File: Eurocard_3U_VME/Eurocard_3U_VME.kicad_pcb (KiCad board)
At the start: 2 copper layers, 100 x 160 mm, 1839 parts, among them J1 VG64_VME_3Rows_3x32_J1_P1

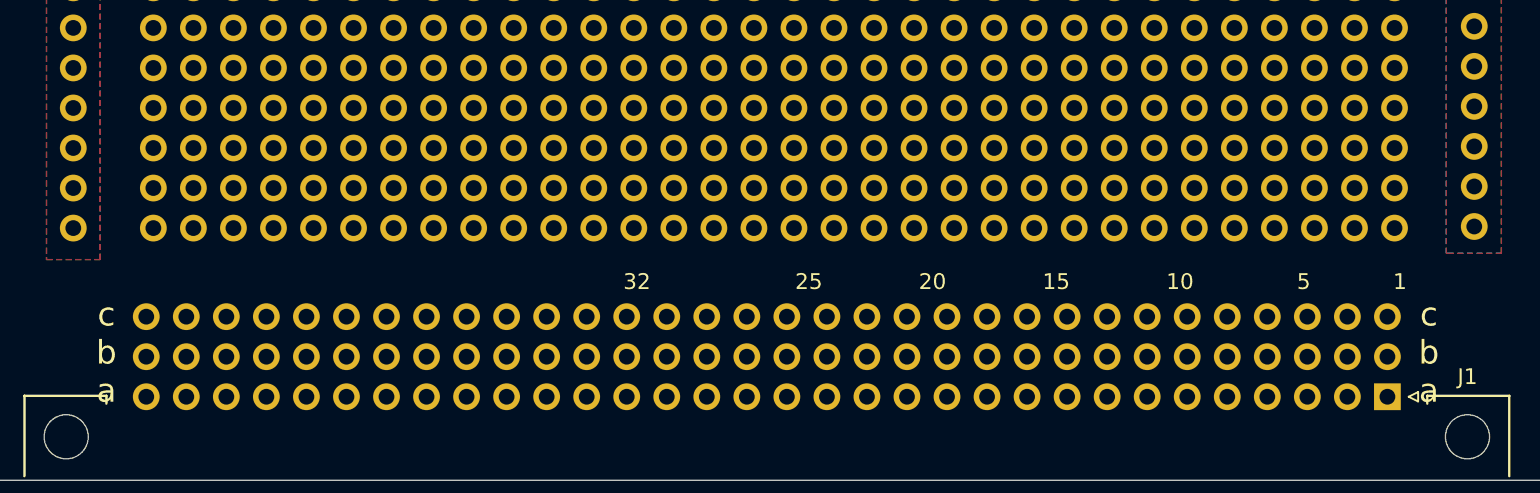
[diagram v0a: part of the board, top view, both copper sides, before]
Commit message: 3U EuroCard VME connector is now breaked out in an identical three rows pattern for easier prototyping
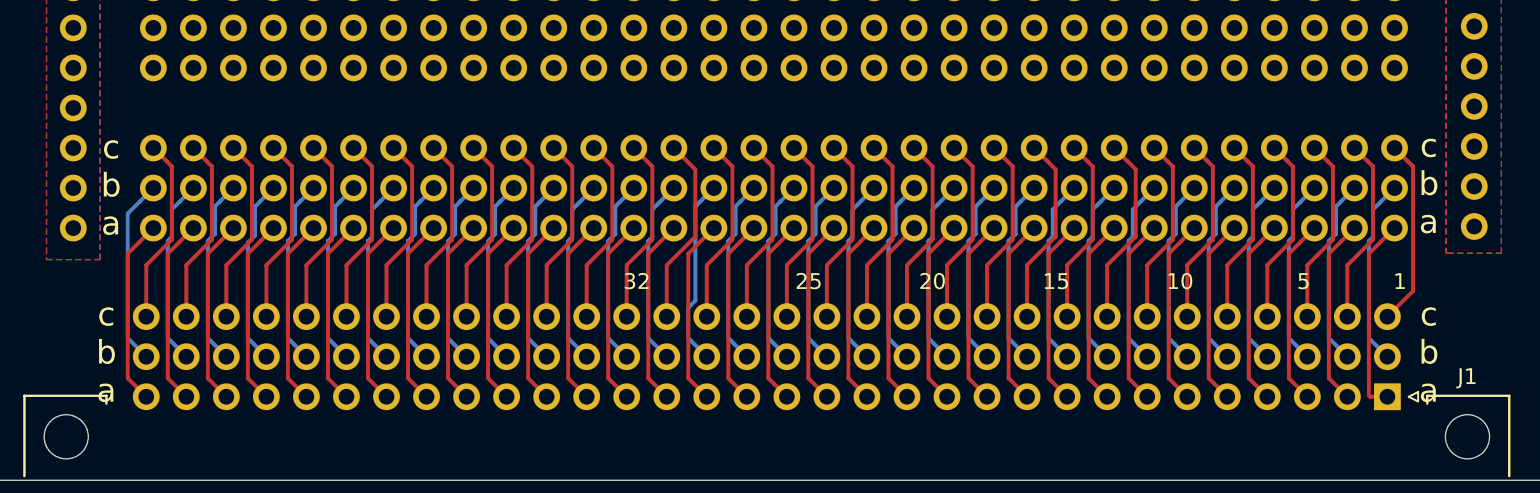
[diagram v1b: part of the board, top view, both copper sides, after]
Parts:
- removed the REF** at (87.3, -23.6)
- removed the REF** at (84.7, -23.6)
- removed the REF** at (82.2, -23.6)
- removed the REF** at (79.7, -23.6)
- removed the REF** at (77.1, -23.6)
- removed the REF** at (74.6, -23.6)
- removed the REF** at (72.0, -23.6)
- removed the REF** at (69.5, -23.6)
- removed the REF** at (67.0, -23.6)
- removed the REF** at (64.4, -23.6)
- removed the REF** at (61.9, -23.6)
- removed the REF** at (59.3, -23.6)
- removed the REF** at (56.8, -23.6)
- removed the REF** at (54.3, -23.6)
- removed the REF** at (51.7, -23.6)
- removed the REF** at (49.2, -23.6)
- removed the REF** at (46.6, -23.6)
- removed the REF** at (44.1, -23.6)
- removed the REF** at (41.6, -23.6)
- removed the REF** at (39.0, -23.6)
- removed the REF** at (36.5, -23.6)
- removed the REF** at (33.9, -23.6)
- removed the REF** at (31.4, -23.6)
- removed the REF** at (28.9, -23.6)
- removed the REF** at (26.3, -23.6)
- removed the REF** at (23.8, -23.6)
- removed the REF** at (21.2, -23.6)
- removed the REF** at (18.7, -23.6)
- removed the REF** at (16.2, -23.6)
- removed the REF** at (13.6, -23.6)
- removed the REF** at (11.1, -23.6)
- removed the REF** at (89.8, -23.6)
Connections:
- REF** pad : (no net) -> Net-(J1-Padc2)
- REF** pad : (no net) -> Net-(J1-Padc3)
- REF** pad : (no net) -> Net-(J1-Padc4)
- REF** pad : (no net) -> Net-(J1-Padc5)
- REF** pad : (no net) -> Net-(J1-Padc6)
- REF** pad : (no net) -> Net-(J1-Padc7)
- REF** pad : (no net) -> Net-(J1-Padc8)
- REF** pad : (no net) -> Net-(J1-Padc9)
- REF** pad : (no net) -> Net-(J1-Padc10)
- REF** pad : (no net) -> Net-(J1-Padc11)
- REF** pad : (no net) -> Net-(J1-Padc12)
- REF** pad : (no net) -> Net-(J1-Padc13)
- REF** pad : (no net) -> Net-(J1-Padc14)
- REF** pad : (no net) -> Net-(J1-Padc15)
- REF** pad : (no net) -> Net-(J1-Padc16)
- REF** pad : (no net) -> Net-(J1-Padc17)
- REF** pad : (no net) -> Net-(J1-Padc18)
- REF** pad : (no net) -> Net-(J1-Padc19)
- REF** pad : (no net) -> Net-(J1-Padc20)
- REF** pad : (no net) -> Net-(J1-Padc21)
- REF** pad : (no net) -> Net-(J1-Padc22)
- REF** pad : (no net) -> Net-(J1-Padc23)
- REF** pad : (no net) -> Net-(J1-Padc24)
- REF** pad : (no net) -> Net-(J1-Padc25)
- REF** pad : (no net) -> Net-(J1-Padc26)
- REF** pad : (no net) -> Net-(J1-Padc27)
- REF** pad : (no net) -> Net-(J1-Padc28)
- REF** pad : (no net) -> Net-(J1-Padc29)
- REF** pad : (no net) -> Net-(J1-Padc30)
- REF** pad : (no net) -> Net-(J1-Padc31)
- REF** pad : (no net) -> Net-(J1-Padc32)
- REF** pad : (no net) -> Net-(J1-Padb2)
- REF** pad : (no net) -> Net-(J1-Padb3)
- REF** pad : (no net) -> Net-(J1-Padb4)
- REF** pad : (no net) -> Net-(J1-Padb5)
- REF** pad : (no net) -> Net-(J1-Padb6)
- REF** pad : (no net) -> Net-(J1-Padb7)
- REF** pad : (no net) -> Net-(J1-Padb8)
- REF** pad : (no net) -> Net-(J1-Padb9)
- REF** pad : (no net) -> Net-(J1-Padb10)
- REF** pad : (no net) -> Net-(J1-Padb11)
- REF** pad : (no net) -> Net-(J1-Padb12)
- REF** pad : (no net) -> Net-(J1-Padb13)
- REF** pad : (no net) -> Net-(J1-Padb14)
- REF** pad : (no net) -> Net-(J1-Padb15)
- REF** pad : (no net) -> Net-(J1-Padb16)
- REF** pad : (no net) -> Net-(J1-Padb17)
- REF** pad : (no net) -> Net-(J1-Padb18)
- REF** pad : (no net) -> Net-(J1-Padb19)
- REF** pad : (no net) -> Net-(J1-Padb20)
- REF** pad : (no net) -> Net-(J1-Padb21)
- REF** pad : (no net) -> Net-(J1-Padb22)
- REF** pad : (no net) -> Net-(J1-Padb23)
- REF** pad : (no net) -> Net-(J1-Padb24)
- REF** pad : (no net) -> Net-(J1-Padb25)
- REF** pad : (no net) -> Net-(J1-Padb26)
- REF** pad : (no net) -> Net-(J1-Padb27)
- REF** pad : (no net) -> Net-(J1-Padb28)
- REF** pad : (no net) -> Net-(J1-Padb29)
- REF** pad : (no net) -> Net-(J1-Padb30)
- REF** pad : (no net) -> Net-(J1-Padb31)
- REF** pad : (no net) -> Net-(J1-Padb32)
- REF** pad : (no net) -> Net-(J1-Pada2)
- REF** pad : (no net) -> Net-(J1-Pada3)
- REF** pad : (no net) -> Net-(J1-Pada4)
- REF** pad : (no net) -> Net-(J1-Pada5)
- REF** pad : (no net) -> Net-(J1-Pada6)
- REF** pad : (no net) -> Net-(J1-Pada7)
- REF** pad : (no net) -> Net-(J1-Pada8)
- REF** pad : (no net) -> Net-(J1-Pada9)
- REF** pad : (no net) -> Net-(J1-Pada10)
- REF** pad : (no net) -> Net-(J1-Pada11)
- REF** pad : (no net) -> Net-(J1-Pada12)
- REF** pad : (no net) -> Net-(J1-Pada13)
- REF** pad : (no net) -> Net-(J1-Pada14)
- REF** pad : (no net) -> Net-(J1-Pada15)
- REF** pad : (no net) -> Net-(J1-Pada16)
- REF** pad : (no net) -> Net-(J1-Pada17)
- REF** pad : (no net) -> Net-(J1-Pada18)
- REF** pad : (no net) -> Net-(J1-Pada19)
- REF** pad : (no net) -> Net-(J1-Pada20)
- REF** pad : (no net) -> Net-(J1-Pada21)
- REF** pad : (no net) -> Net-(J1-Pada22)
- REF** pad : (no net) -> Net-(J1-Pada23)
- REF** pad : (no net) -> Net-(J1-Pada24)
- REF** pad : (no net) -> Net-(J1-Pada25)
- REF** pad : (no net) -> Net-(J1-Pada26)
- REF** pad : (no net) -> Net-(J1-Pada27)
- REF** pad : (no net) -> Net-(J1-Pada28)
- REF** pad : (no net) -> Net-(J1-Pada29)
- REF** pad : (no net) -> Net-(J1-Pada30)
- REF** pad : (no net) -> Net-(J1-Pada31)
- REF** pad : (no net) -> Net-(J1-Pada32)
- REF** pad : (no net) -> Net-(J1-Padc1)
- REF** pad : (no net) -> Net-(J1-Padb1)
- REF** pad : (no net) -> Net-(J1-Pada1)
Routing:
- net Net-(J1-Pada1): track 0.00 -> 12.5 mm
- net Net-(J1-Padc10): track 0.00 -> 12.0 mm
- net Net-(J1-Padc8): track 0.00 -> 12.0 mm
- net Net-(J1-Padc19): track 0.00 -> 12.0 mm
- net Net-(J1-Padb8): track 0.00 -> 11.9 mm
- net Net-(J1-Pada8): track 0.00 -> 11.9 mm
- net Net-(J1-Padc5): track 0.00 -> 11.9 mm
- net Net-(J1-Padb3): track 0.00 -> 11.9 mm
- net Net-(J1-Padb13): track 0.00 -> 11.9 mm
- net Net-(J1-Padb10): track 0.00 -> 11.9 mm
- net Net-(J1-Padb1): track 0.00 -> 11.9 mm
- net Net-(J1-Pada3): track 0.00 -> 11.9 mm
- net Net-(J1-Pada13): track 0.00 -> 11.9 mm
- net Net-(J1-Pada12): track 0.00 -> 11.9 mm
- net Net-(J1-Pada10): track 0.00 -> 11.9 mm
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
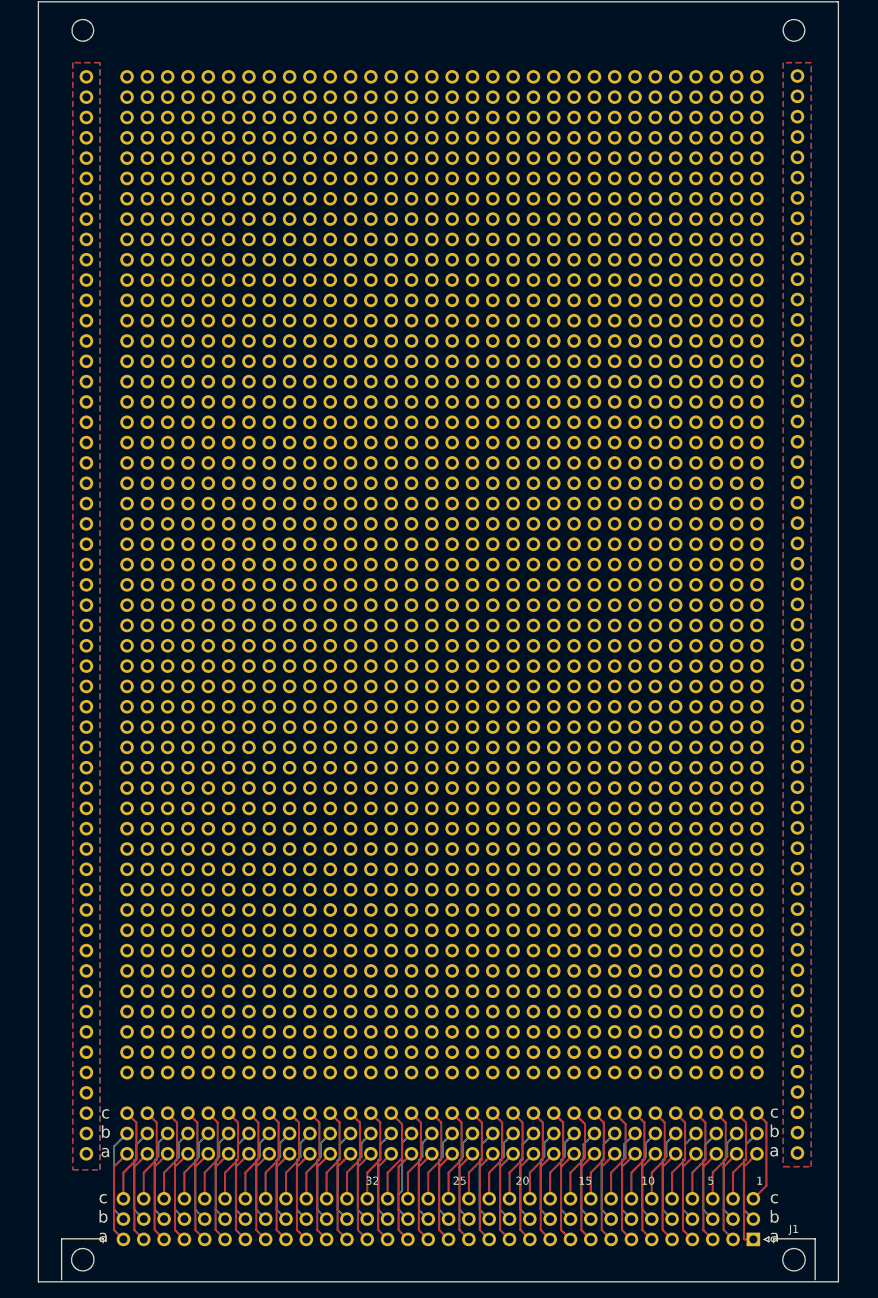
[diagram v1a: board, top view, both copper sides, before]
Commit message: Added grids
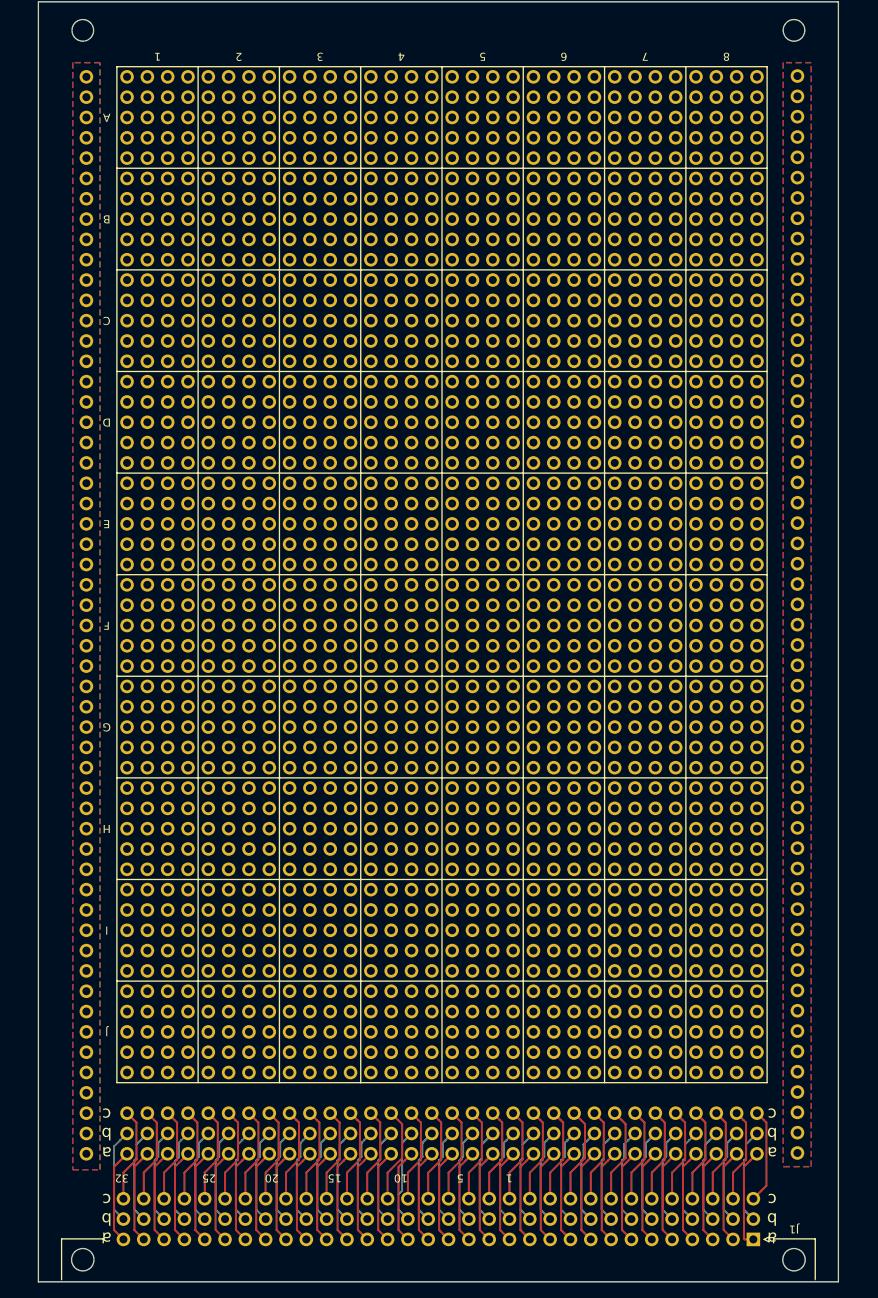
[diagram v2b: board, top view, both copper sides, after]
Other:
- board text added: "1"
- board text added: "1 5 10 15 20 25 32"
- board text added: "2"
- board text added: "3"
- board text added: "4"
- board text added: "5"
- board text added: "6"
- board text added: "7"
- board text added: "8"
- board text added: "A"
- board text added: "B"
- board text added: "C"
- board text added: "D"
- board text added: "E"
- board text added: "F"
- board text added: "G"
- board text added: "H"
- board text added: "I"
- board text added: "J"
- board text added: "a b c"
- board text added: "keepout areas on both sides for board guides 50 x 32 holes"
- board text removed: "c b a"
- board text removed: "keepout areas on both sides for board guides 88 x 55 holes"

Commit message: Move board, replot
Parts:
- moved J1 201.8 mm to (151.3, 186.7)
- moved REF** 201.8 mm to (151.8, 165.9)
- moved REF** 201.8 mm to (146.7, 41.4)
- moved REF** 201.8 mm to (95.9, 51.6)
- moved REF** 201.8 mm to (113.7, 122.7)
- moved REF** 201.8 mm to (111.2, 122.7)
- moved REF** 201.8 mm to (108.6, 122.7)
- moved REF** 201.8 mm to (106.1, 122.7)
- moved REF** 201.8 mm to (103.5, 122.7)
- moved REF** 201.8 mm to (101.0, 122.7)
- moved REF** 201.8 mm to (98.5, 122.7)
- moved REF** 201.8 mm to (95.9, 122.7)
- moved REF** 201.8 mm to (93.4, 122.7)
- moved REF** 201.8 mm to (90.8, 122.7)
- moved REF** 201.8 mm to (93.4, 51.6)
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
